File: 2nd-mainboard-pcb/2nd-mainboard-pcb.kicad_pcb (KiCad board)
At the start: 4 copper layers, 99 x 97.5 mm, 131 parts, among them J1 PJ-082BH, J10 Servo Motor BL Touch, J11 T3, J12 Steckverbinder_Male_Fans, J13 Steckverbinder_Female_Leistung, J14 FAN3, J15 Steckverbinder_Female_Motoren, J16 ISP, J18 Quartz, J19 T2, J2 Fan_12/5V_Regelung, J20 T2, J21 T2, J22 T3, J23 Conn_01x04_Socket, J24 Steckverbinder_Male_Leistung, J3 Fan_12/5V_Regelung, J4 FAN0, J5 FAN1, J6 FAN2, J7 Stepper Motor, J8 Servo Motor SM, J9 Microstepping, P1 USB_C_Receptacle_USB2.0_14P, SW3 PTS820 J25K SMTR LFS, U1 SQJ409EP-T1_GE3, U10 ATmega328PB-A, U12 MPU-6050, U2 SZ1SMB5927BT3G, U4 TPS565208, U5 FT232RL, U6 TPS56837RPAR, U7 TPM16050-S6TR, U8 RJK0456DPB-00-J5, U9 RJK0456DPB-00-J5, Y1 ECS-160-18-4X-CKM

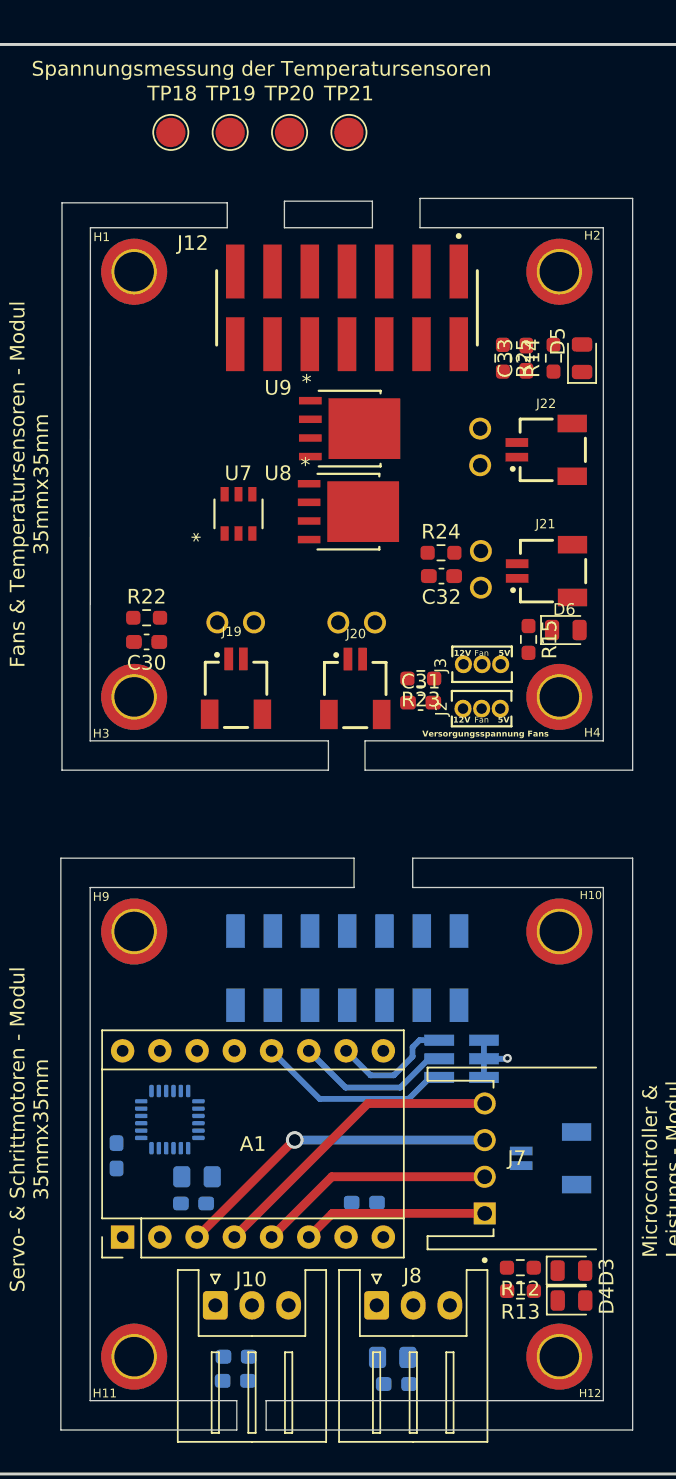
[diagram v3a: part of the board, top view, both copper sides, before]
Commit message: motor module traced
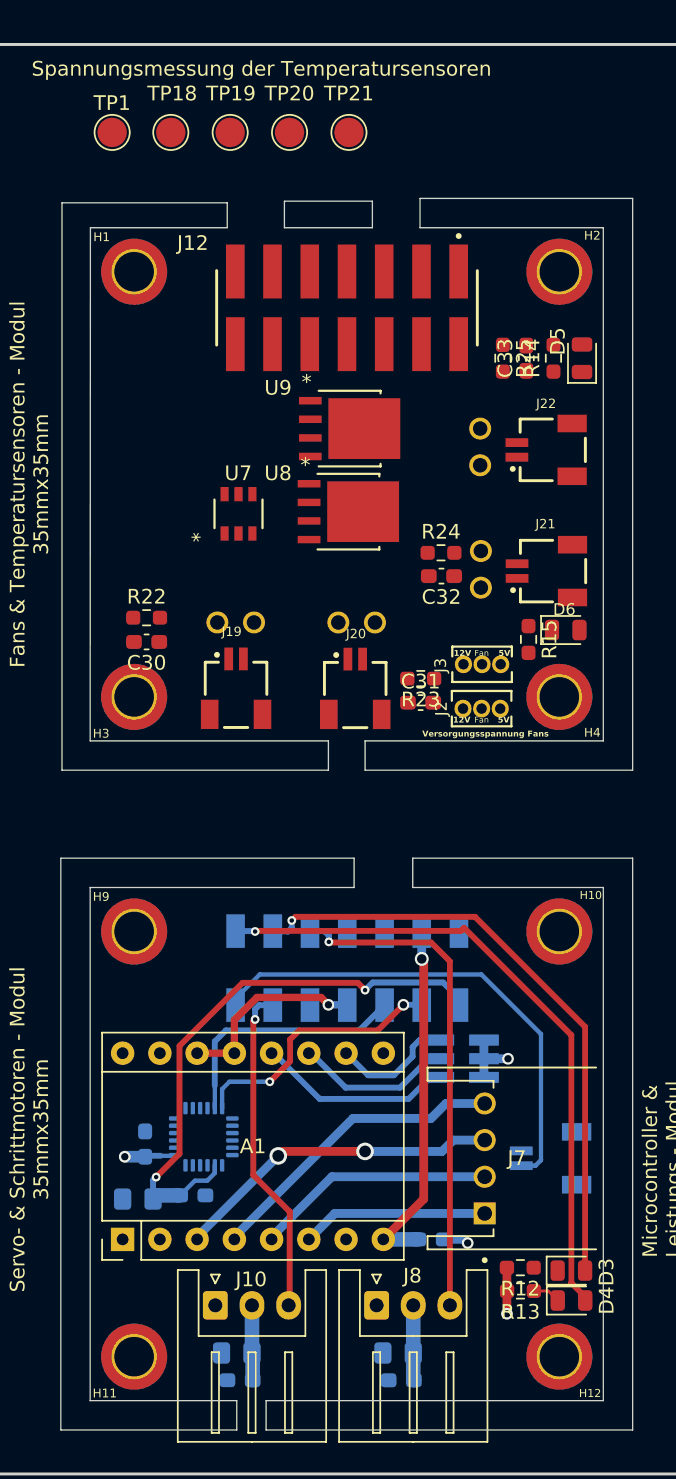
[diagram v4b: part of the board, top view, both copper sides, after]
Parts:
- added TP1: ADC0, TestPoint:TestPoint_Pad_D2.0mm, F.Cu at (59.0, 58.5)
- C28: footprint Capacitor_SMD:C_0603_1608Metric_Pad1.08x0.95mm_HandSolder -> Capacitor_SMD:C_0805_2012Metric_Pad1.18x1.45mm_HandSolder
- moved C23 5.19 mm to (80.8, 134.0), turned to 0 degrees
- moved C34 4.31 mm to (60.8, 131.2), turned to 180 degrees
- moved U12 2.59 mm to (65.2, 127.0)
- moved C27 2.11 mm to (61.2, 127.5), turned to 90 degrees
- moved C35 0.55 mm to (64.5, 131.0)
- moved C25 0.47 mm to (78.5, 141.8)
- moved C26 0.42 mm to (78.7, 143.6)
- moved C29 0.33 mm to (67.7, 143.6)
- moved C28 0.25 mm to (67.5, 141.8)
- moved A1 0.16 mm to (59.7, 134.0)
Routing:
- net LED_MOT0: track 21.9 -> 66.4 mm, vias 0 -> 1
- net LED_MOT1: track 20.4 -> 62.2 mm, vias 2 -> 3
- net AREF: track 43.8 -> 82.6 mm, vias 6 -> 8
- net MOSI: track 20.8 -> 54.9 mm, vias 2 -> 3
- net BLT_Switch: track 9.39 -> 43.1 mm
- net +12V: track 22.8 -> 47.4 mm, vias 4 -> 5
- net BLT_Servo: track 8.50 -> 31.1 mm, vias 0 -> 1
- net SDA: track 9.28 -> 27.5 mm, vias 0 -> 2
- net SCL: track 7.58 -> 24.7 mm
- net +5V_POW: track 36.4 -> 50.1 mm, vias 6 -> 7
- net RESET: track 89.9 -> 103.2 mm, vias 5 -> 6
- net GND: track 124.2 -> 130.7 mm, vias 17 -> 19
- net Net-(D4-K): track 0.00 -> 1.90 mm
- net STP_A2: track 22.4 -> 22.5 mm, vias 1 -> 2

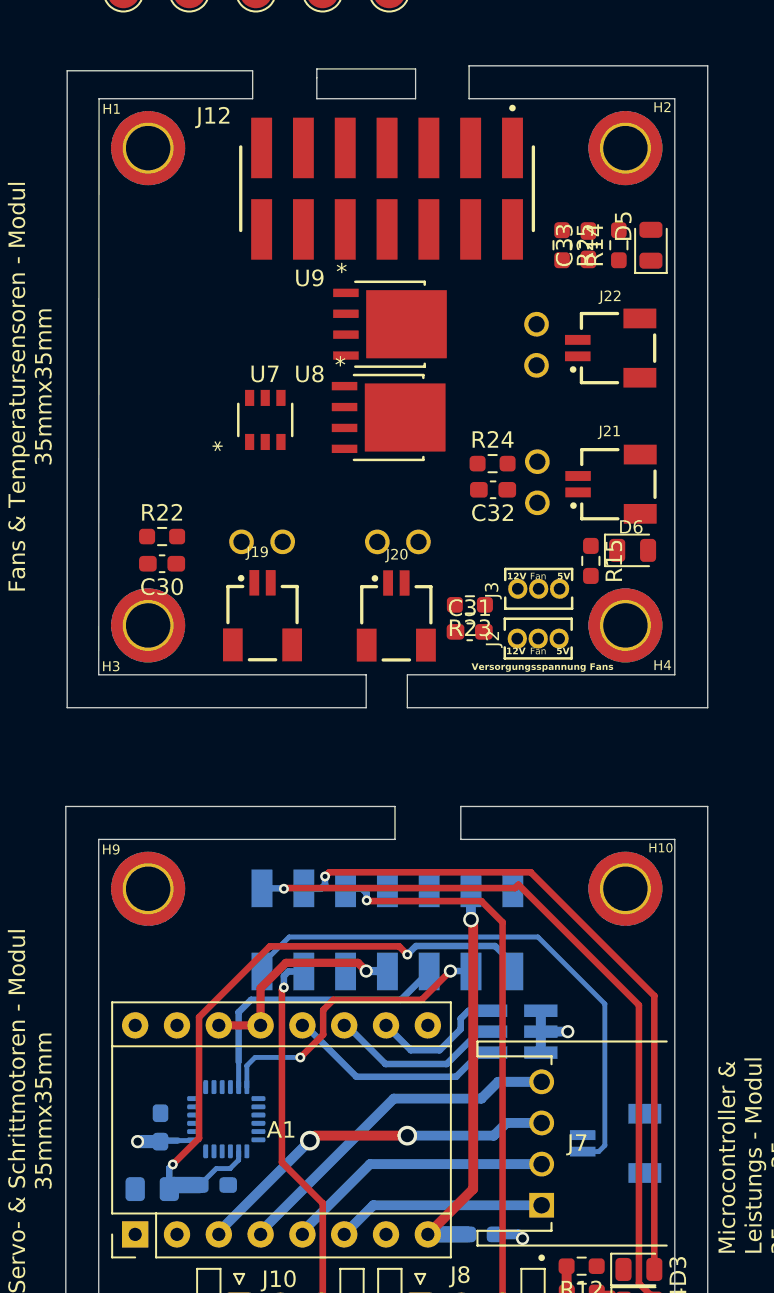
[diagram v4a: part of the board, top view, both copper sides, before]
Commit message: finished Fan-module tracing, now checking ground connections and integrating test-plattform
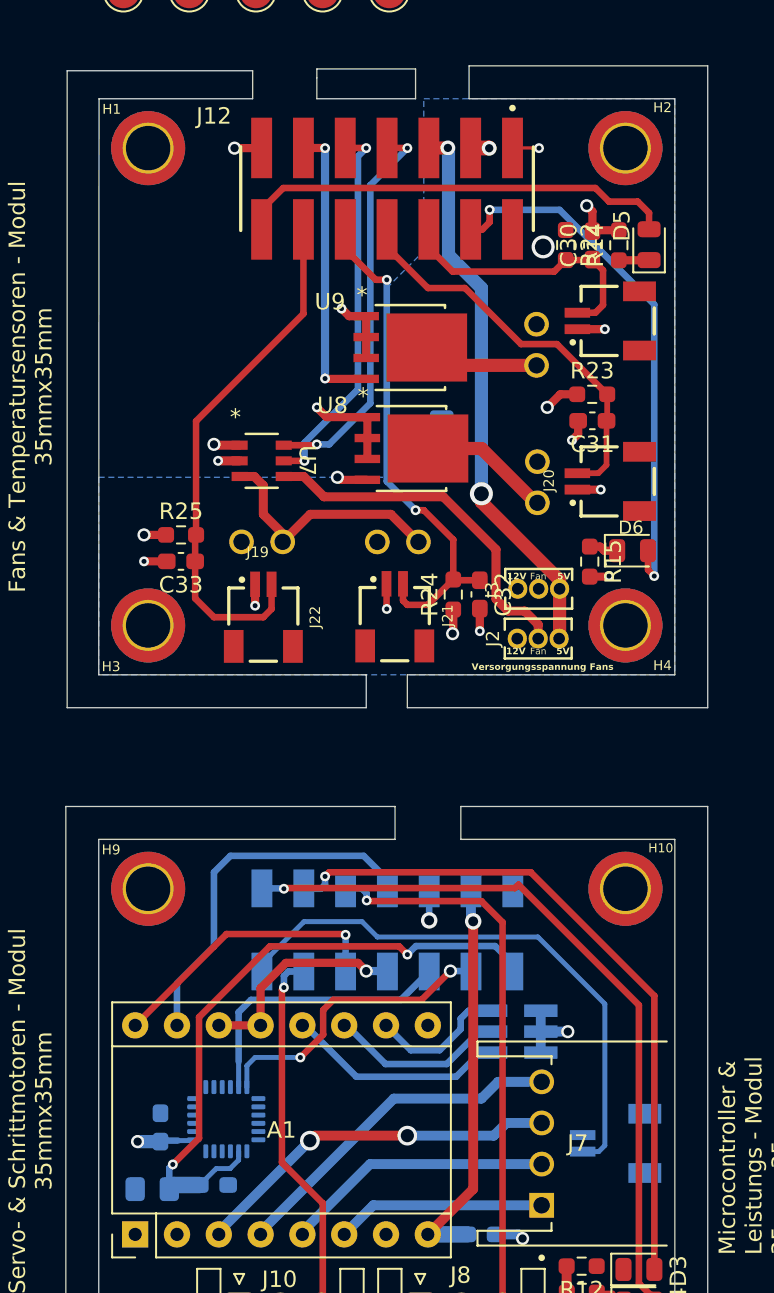
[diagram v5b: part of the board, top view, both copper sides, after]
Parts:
- moved C30 32.5 mm to (87.5, 73.9), turned to 90 degrees
- moved C33 31.3 mm to (62.5, 93.1), turned to 180 degrees
- moved R22 30.3 mm to (85.9, 73.9), turned to -90 degrees
- moved R25 29.1 mm to (62.5, 91.5), turned to 0 degrees
- moved J19 27.6 mm to (88.5, 78.5), turned to 90 degrees
- moved J22 26.6 mm to (67.5, 96.4), turned to 0 degrees
- moved J21 15.3 mm to (75.5, 96.4), turned to 0 degrees
- moved J20 15.2 mm to (88.5, 88.2), turned to 90 degrees
- moved C31 14.8 mm to (87.5, 84.6), turned to 180 degrees
- moved R23 14.8 mm to (87.5, 83.0), turned to 0 degrees
- moved R24 8.30 mm to (79.0, 95.1), turned to 90 degrees
- moved C37 7.72 mm to (76.3, 85.8), turned to 90 degrees
- moved C32 6.41 mm to (80.7, 95.1), turned to -90 degrees
- moved C36 5.97 mm to (78.3, 85.6), turned to 90 degrees
- moved U7 2.49 mm to (67.4, 87.0), turned to 0 degrees
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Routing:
- net +5V_POW: track 50.1 -> 85.9 mm, vias 7 -> 10
- net LED_FAN1: track 14.6 -> 47.2 mm, vias 1 -> 3
- net ADC3: track 10.1 -> 42.1 mm
- net ADC2: track 10.1 -> 41.3 mm, vias 1 -> 3
- net GND: track 130.7 -> 158.2 mm, vias 19 -> 32
- net LED_FAN0: track 14.6 -> 41.5 mm
- net ADC1: track 8.20 -> 32.6 mm
- net FAN_01_PWM_clockwise: track 20.3 -> 44.3 mm, vias 1 -> 3
- net FAN_01_PWM_counterclockwise: track 20.2 -> 43.3 mm, vias 1 -> 3
- net STEP: track 34.4 -> 56.7 mm
- net Fan_Versorgung_01: track 0.00 -> 21.8 mm
- net FAN_3_PWM: track 19.5 -> 37.3 mm, vias 1 -> 3
- net DIR: track 5.60 -> 22.9 mm, vias 0 -> 1
- net ADC0: track 8.31 -> 25.0 mm
- net Net-(U7-OUT1): track 0.00 -> 15.2 mm
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- added copper zone on B.Cu, net AREF
- added copper zone on In2.Cu, net FAN_2_PWM
- added copper zone on In2.Cu, net Fan_Versorgung_23
- added copper zone on In2.Cu, net Net-(U7-OUT2)

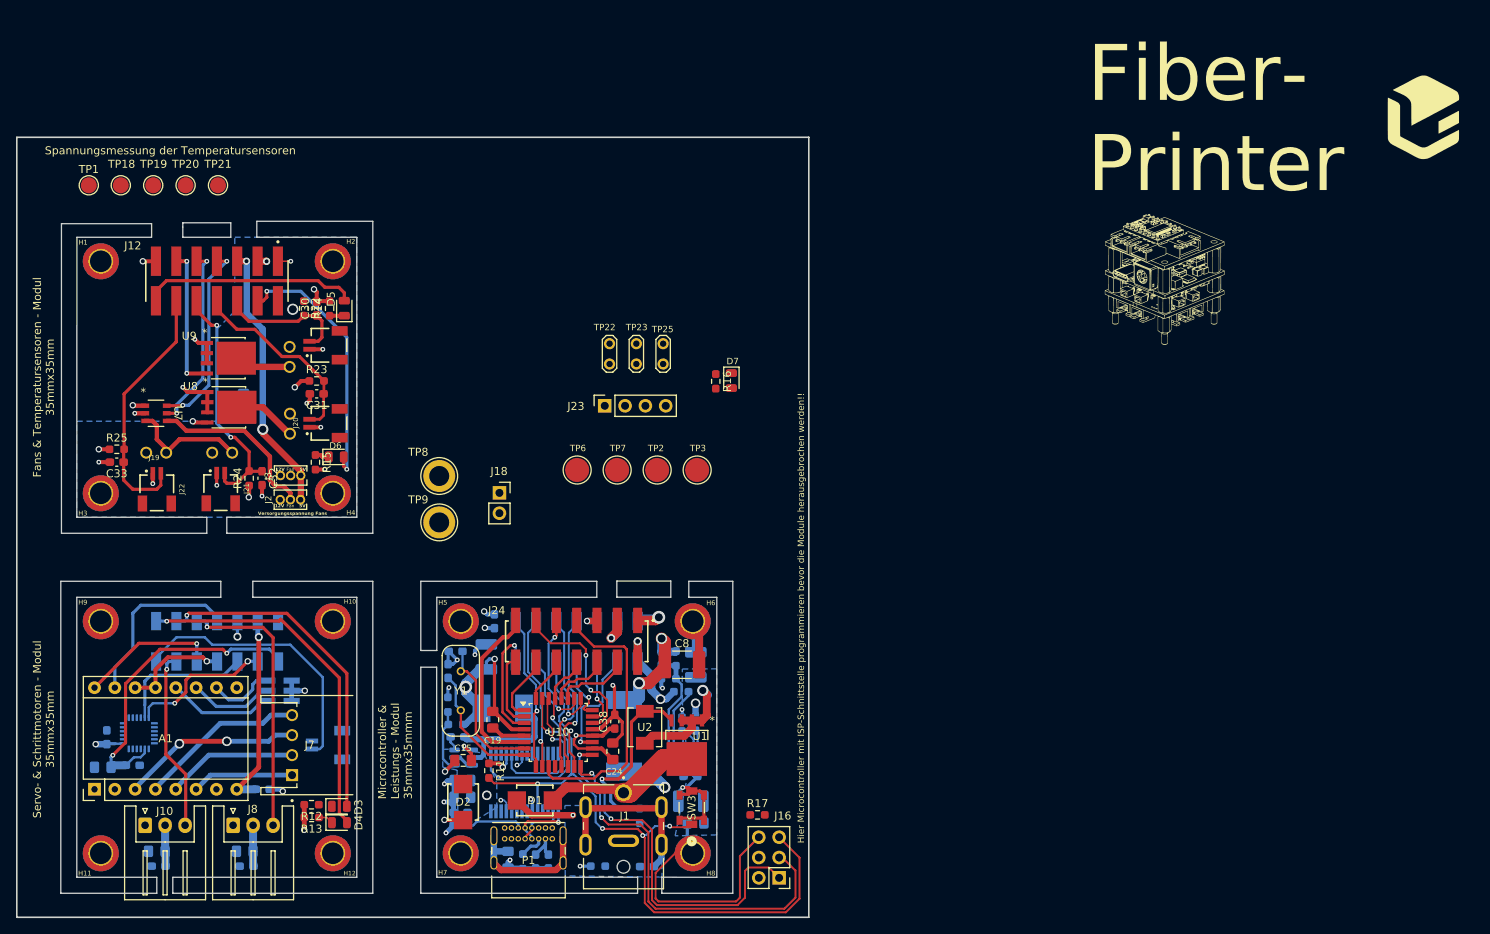
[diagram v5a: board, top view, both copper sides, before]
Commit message: finished all traces, 59 drc check errors to go
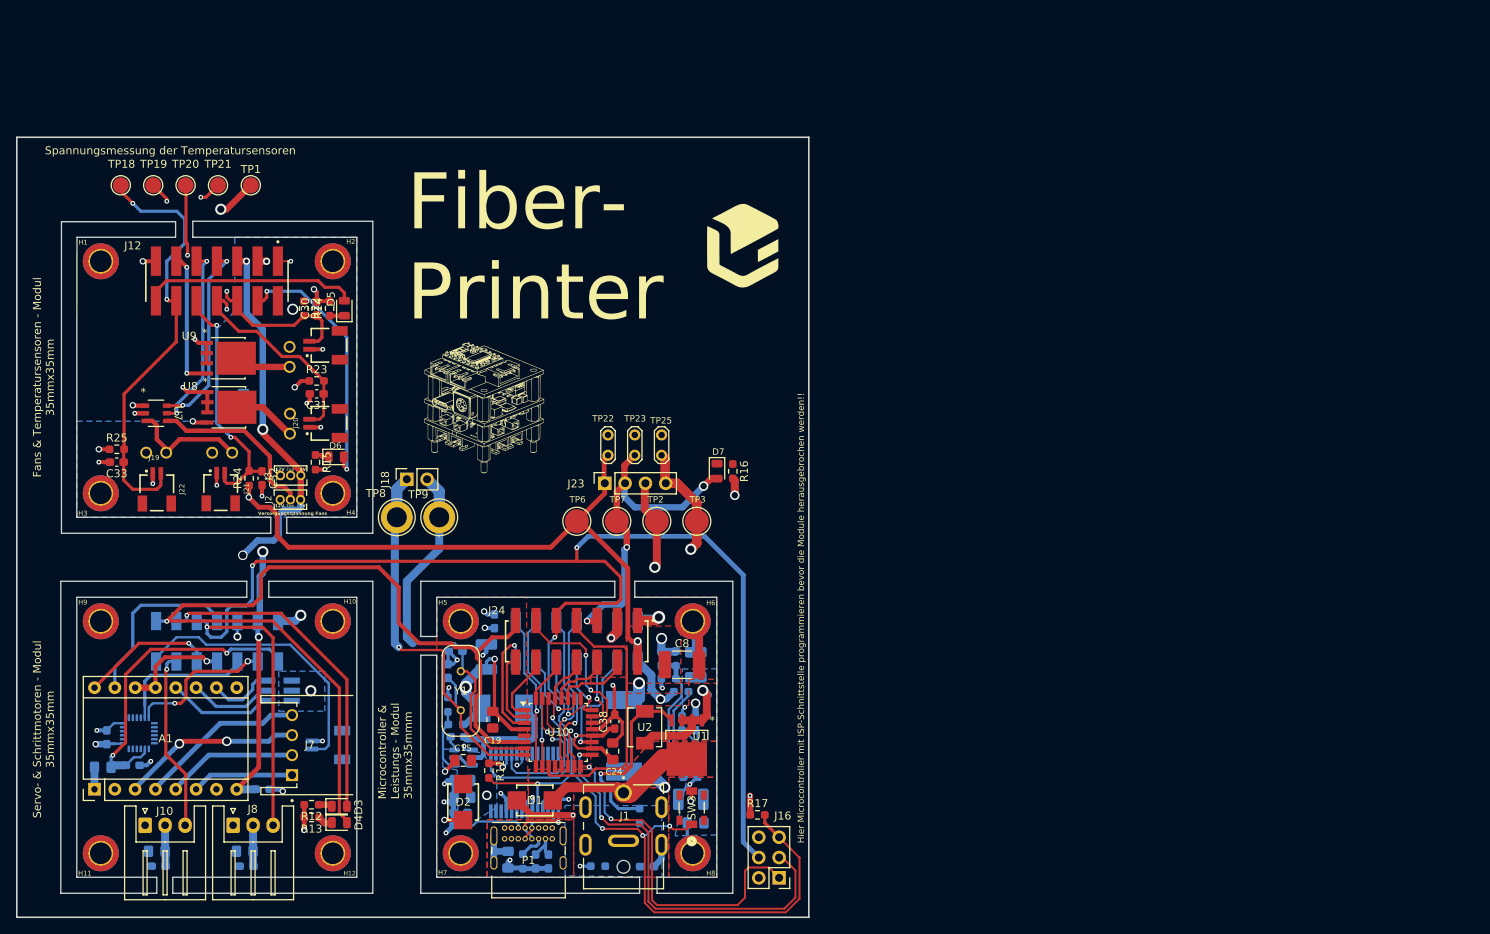
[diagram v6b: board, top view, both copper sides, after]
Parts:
- moved G*** 86.6 mm to (108.4, 86.3)
- moved G*** 86.6 mm to (140.8, 65.9)
- moved TP1 20.2 mm to (79.2, 58.5)
- moved J18 11.7 mm to (98.8, 95.2), turned to 90 degrees
- moved D7 11.5 mm to (137.5, 94.2)
- moved R16 11.4 mm to (139.5, 94.2)
- moved TP23 11.4 mm to (127.2, 92.2)
- moved TP25 11.4 mm to (130.6, 92.2)
- moved TP22 11.4 mm to (123.9, 92.2)
- moved J23 9.68 mm to (123.5, 95.8)
- moved TP8 7.40 mm to (97.5, 100.0)
- moved TP2 6.41 mm to (130.0, 100.5)
- moved TP3 6.41 mm to (135.0, 100.5)
- moved TP6 6.41 mm to (120.0, 100.5)
- moved TP7 6.41 mm to (125.0, 100.5)
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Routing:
- net GND: track 158.2 -> 317.5 mm, vias 32 -> 41
- net +5V_POW: track 85.9 -> 243.6 mm, vias 10 -> 14
- net MOSI: track 54.9 -> 190.2 mm, vias 3 -> 5
- net +12V: track 48.6 -> 137.2 mm, vias 6 -> 8
- net AREF: track 87.6 -> 163.7 mm
- net LED_MOT0: track 66.4 -> 117.5 mm
- net Quartz_1: track 16.2 -> 52.0 mm, vias 0 -> 1
- net Quartz_2: track 18.4 -> 48.6 mm
- net ADC3: track 42.1 -> 64.5 mm, vias 1 -> 3
- net ADC2: track 41.3 -> 62.1 mm, vias 3 -> 4
- net ADC0: track 25.0 -> 45.1 mm, vias 1 -> 3
- net ADC1: track 32.6 -> 52.3 mm, vias 1 -> 3
- net GND3: track 22.1 -> 3.12 mm
- net Net-(P1-SHIELD): track 19.3 -> 6.56 mm
- net RESET: track 103.2 -> 107.2 mm
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- added copper zone on F.Cu, net +12V
- added copper zone on F.Cu, net +24V
- added copper zone on B.Cu, net +5V_POW
- added copper zone on F.Cu, net GND
- added copper zone on F.Cu, net GND3
- added copper zone on F.Cu, net Net-(P1-SHIELD)
- added copper zone on F.Cu, net PWR_IN_PROT
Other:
- outline, holes or cut-outs redrawn
